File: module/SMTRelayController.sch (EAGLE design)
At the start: 34 parts, among them Q1 2n3904, Q2 2n3904, Q3 2n3904, U1 L298

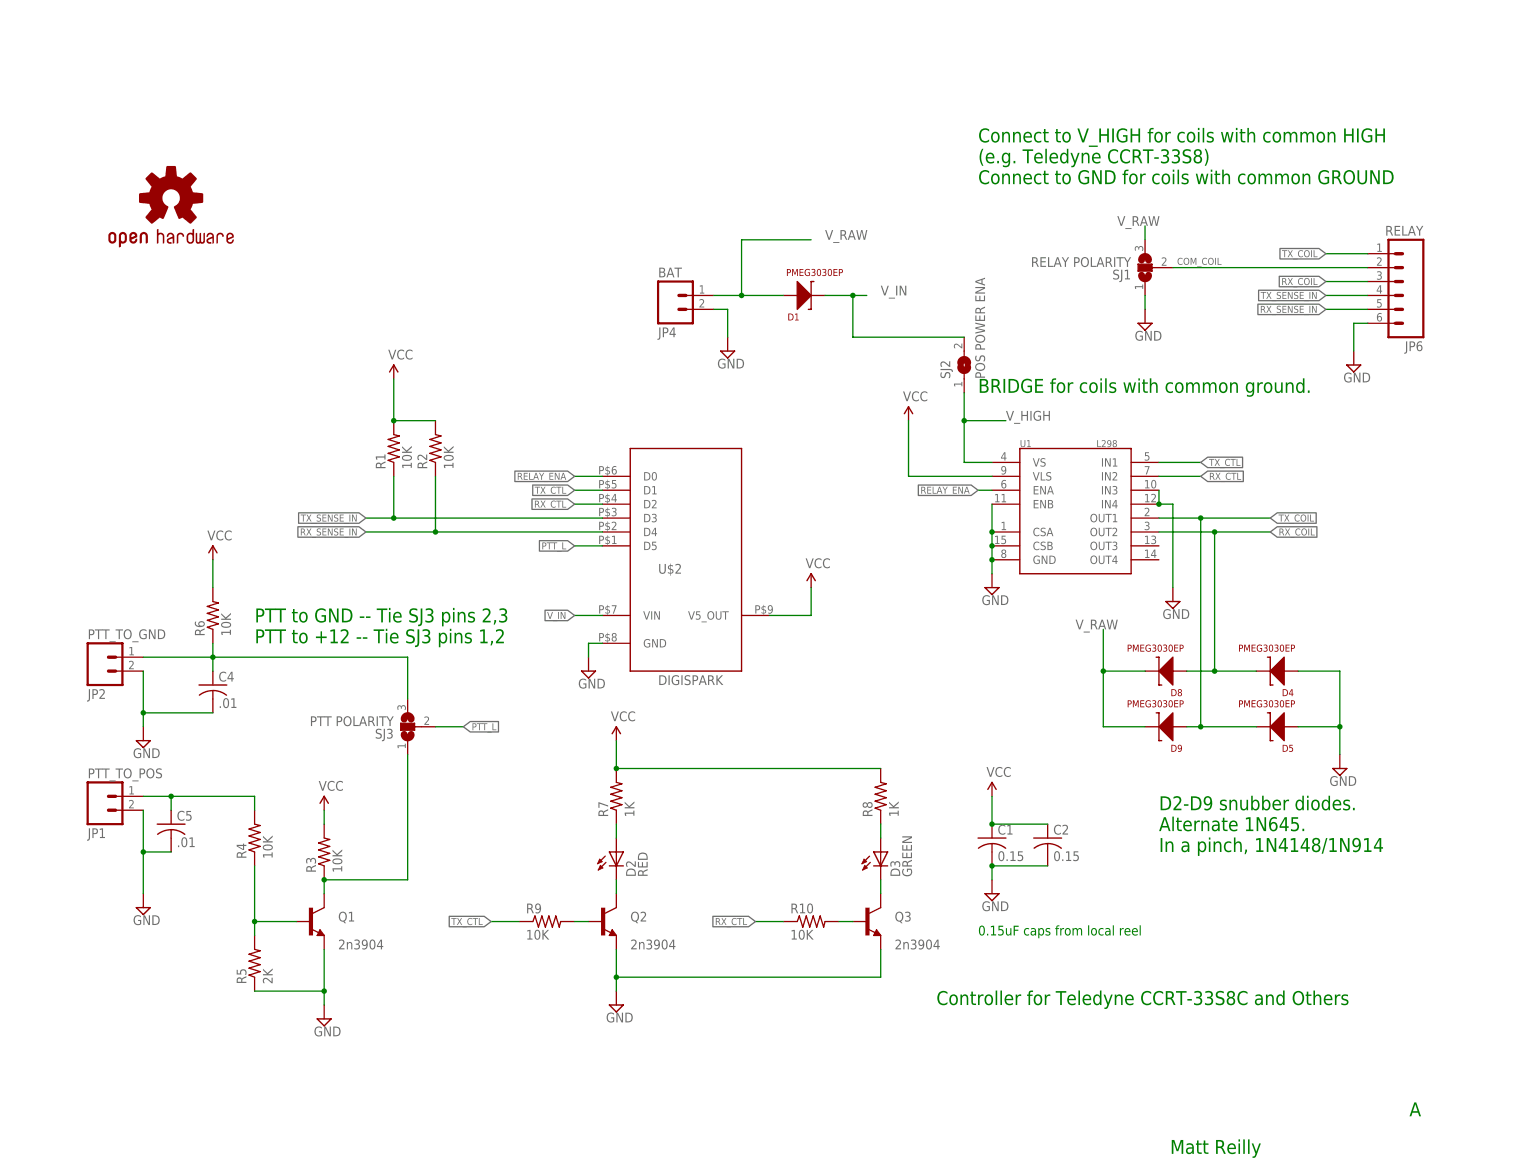
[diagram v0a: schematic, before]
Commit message: Updates with OSHW logo, surface mount parts, and improved PTT2GND (protected) circuit.
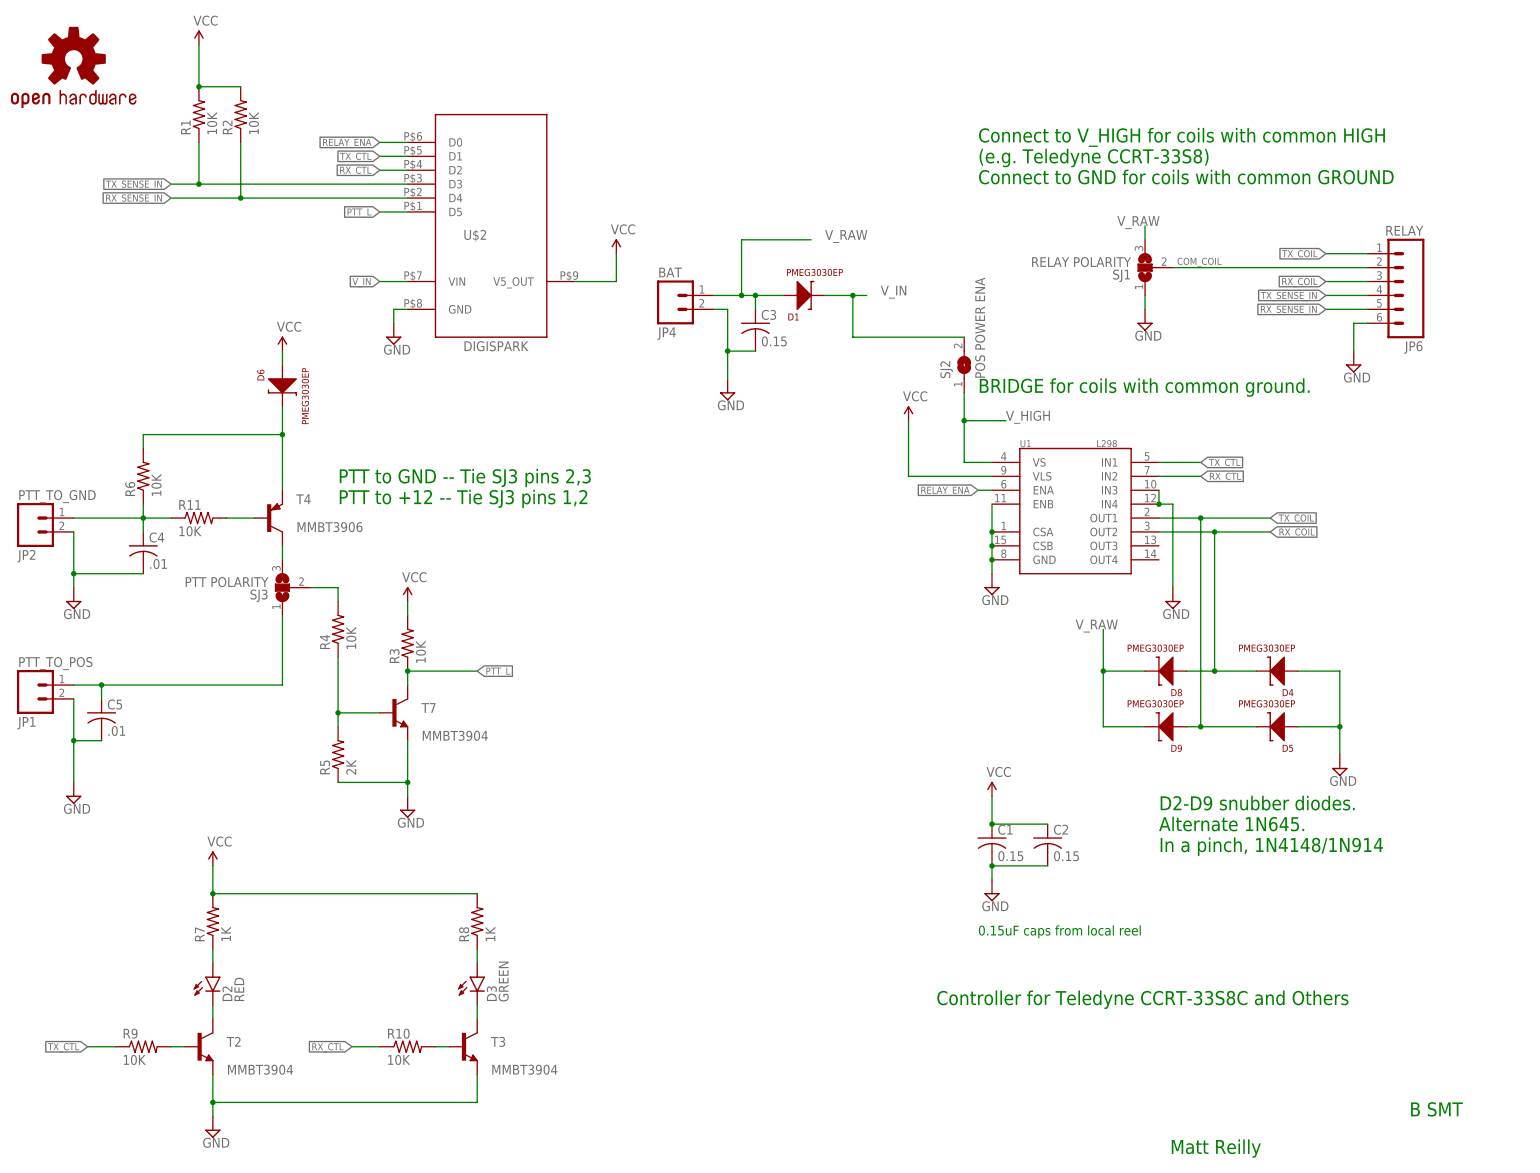
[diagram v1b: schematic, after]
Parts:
- removed Q1, Q2, Q3: 2n3904, transistor:2N3904
- added C3: 0.15, resistor:C-USC1206K
- added D6: PMEG3030EP, kb1vc_robot_parts:PMEG3030EP
- added R11: 10K, rcl:R-US_R1206
- added T2, T3, T7: MMBT3904, transistor-neu-to92:MMBT3904LT1-NPN-SOT23-BEC
- added T4: MMBT3906, transistor-neu-to92:MMBT3906LT1-PNP-SOT23-BEC
- D2, D3: device led:LED3MM -> SparkFun-LED:LED1206
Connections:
- new net N$11: C4.1, JP2.1, R11.1, R6.1
- new net N$12: D6.C, R6.2, T4.E
- new net N$13: SJ3.3, T4.C
- net GND: now also C3.2, T2.E, T3.E, T7.E; no longer Q1.E, Q2.E, Q3.E
- net N$1: now also SJ3.1; no longer R4.2
- net N$10: now also T3.B; no longer Q3.B
- net N$2: now also R4.2, SJ3.2; no longer Q1.C, R3.1, SJ3.1
- net N$4: now also T7.B; no longer Q1.B
- net N$5: now also R11.2, T4.B; no longer C4.1, JP2.1, R6.1, SJ3.3
- net N$7: now also T2.C; no longer Q2.C
- net N$8: now also T3.C; no longer Q3.C
- net N$9: now also T2.B; no longer Q2.B
- net PTT_L: now also R3.1, T7.C; no longer SJ3.2
- net VCC: now also D6.A; no longer R6.2
- net V_RAW: now also C3.1
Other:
- note added: "B SMT"
- note removed: "A"
- moved on the sheet: C4, C5, JP1, JP2, R1, R10, R2, R3, R4, R5, R6, R7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
